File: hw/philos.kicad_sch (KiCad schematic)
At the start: 3 parts, among them U1 8086_Min_Mode, U2 SN74AHC574N, U3 SN74AHC574N

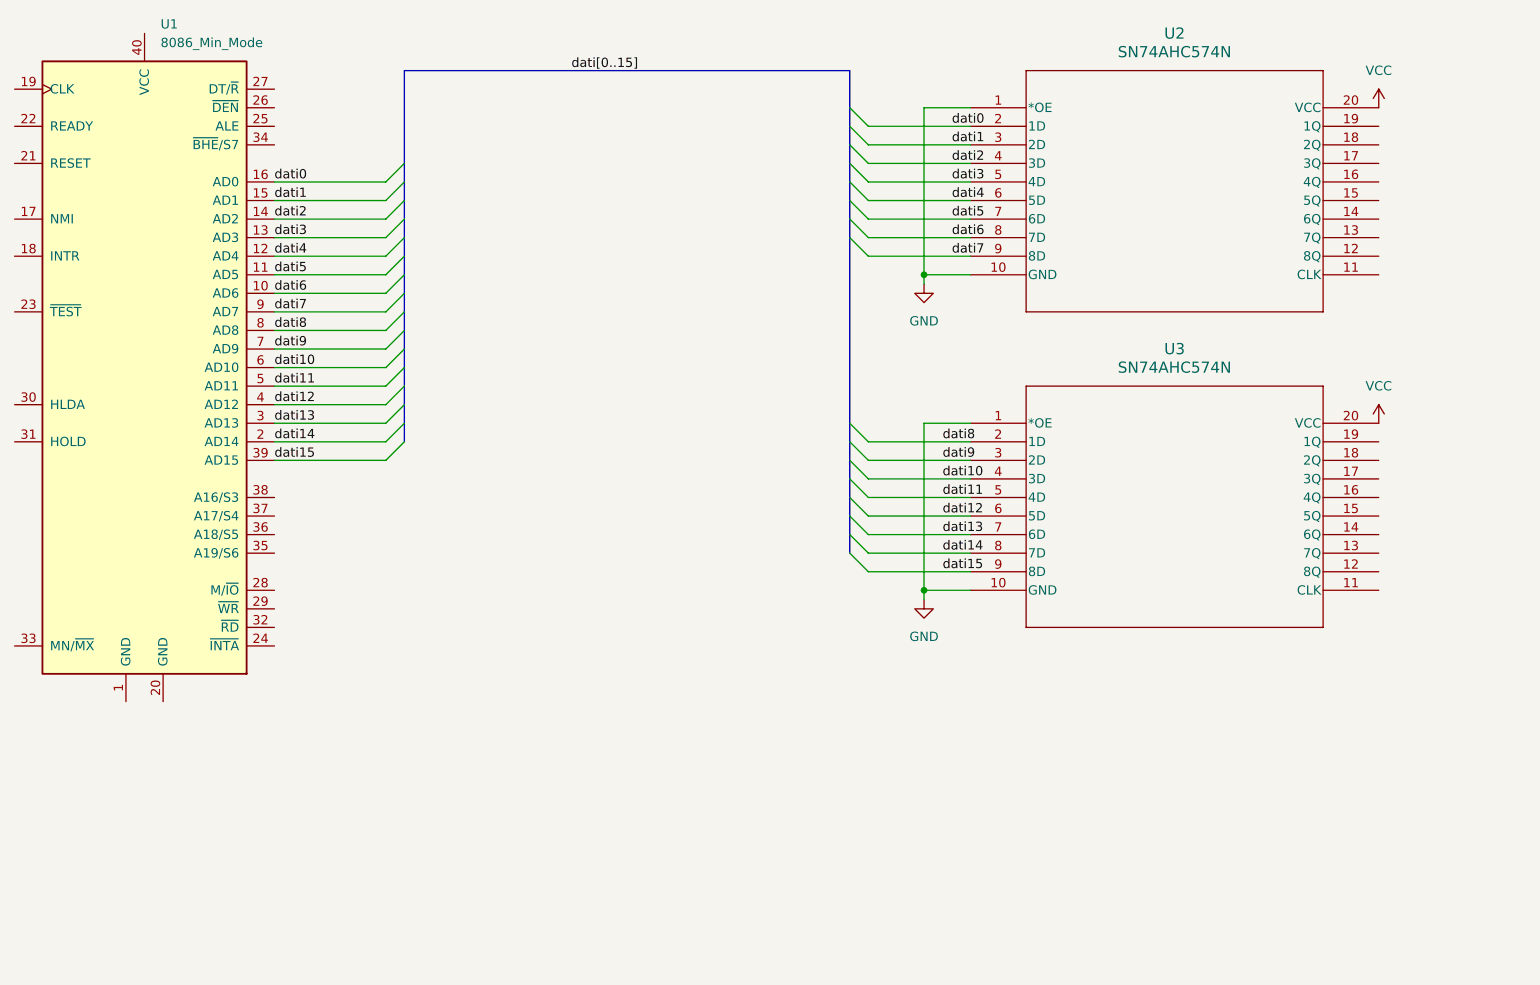
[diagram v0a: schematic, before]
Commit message: hw: Update to Kicad 9.0; Create makefile prototype; Remove batch script
The makefile is still in beta, needs more work

Signed-off-by: Matteo Bertolino <m.bertolino.m@gmail.com>
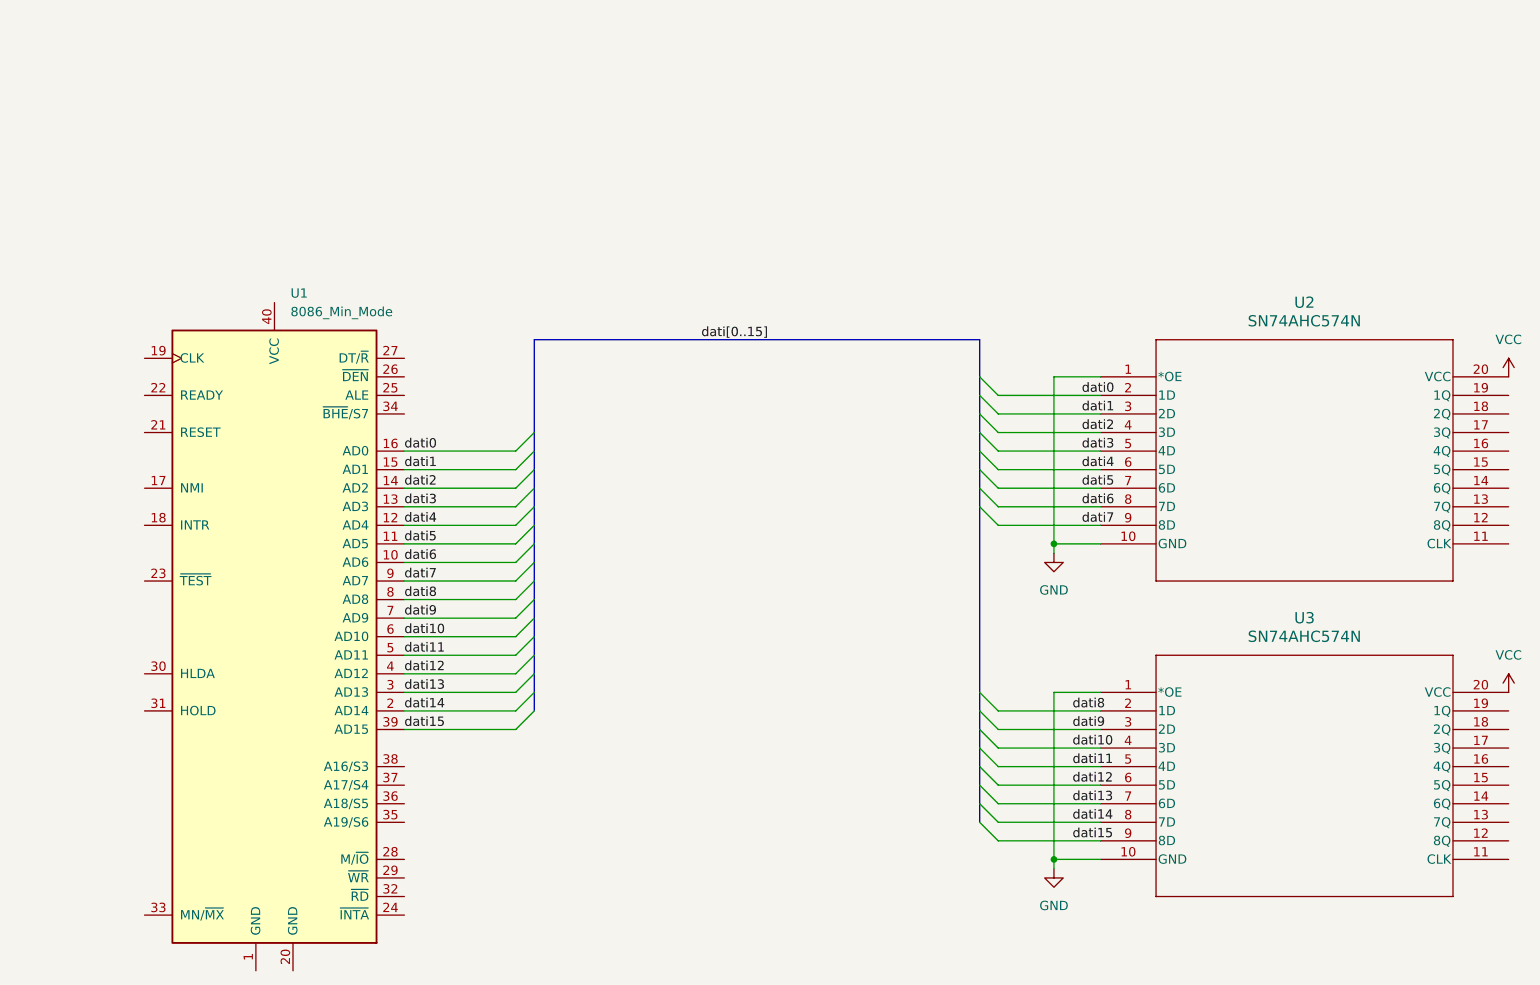
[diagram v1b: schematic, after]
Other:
- title: (none) -> philOS
- moved on the sheet: U1, U2, U3

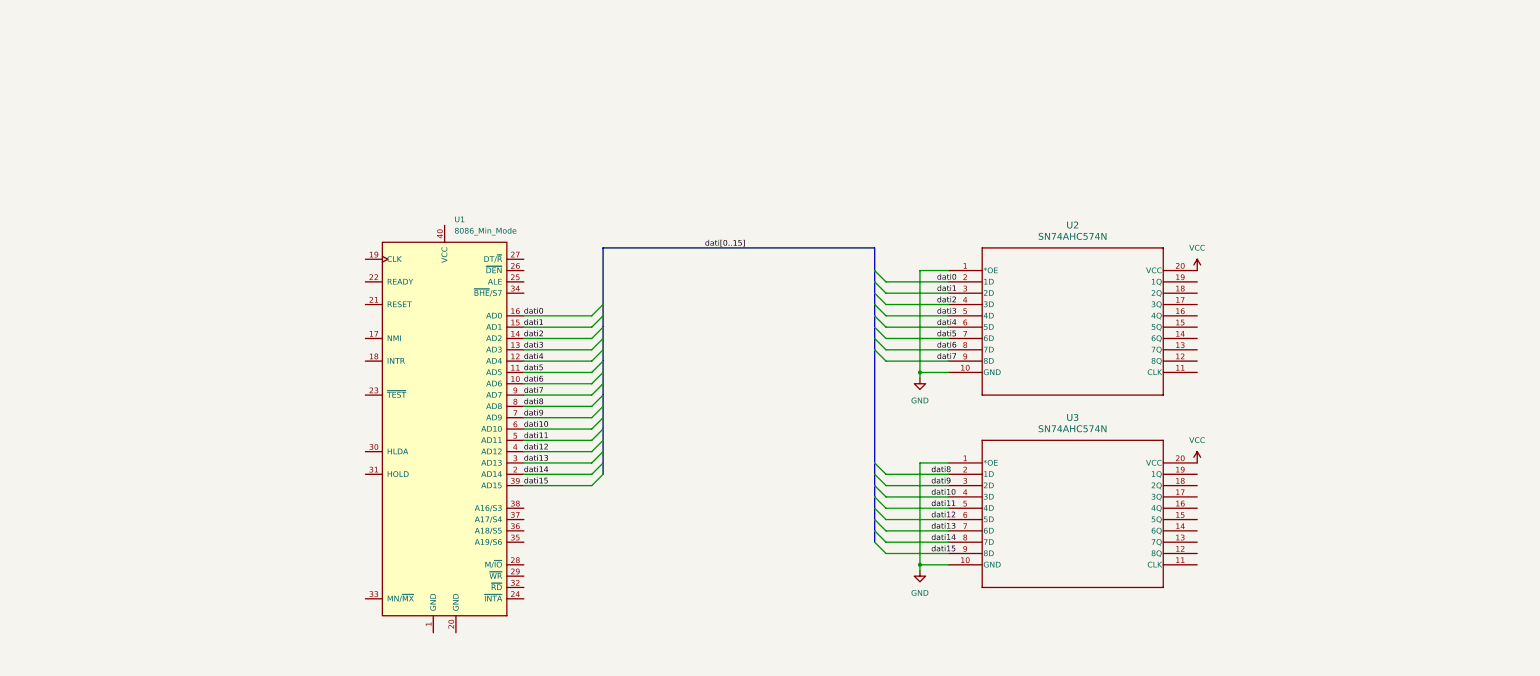
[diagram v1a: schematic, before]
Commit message: hw: add EEPROM and clock with respective footprints and symbols in diagram
No connection between component has been made yet

Signed-off-by: Matteo Bertolino <m.bertolino.m@gmail.com>
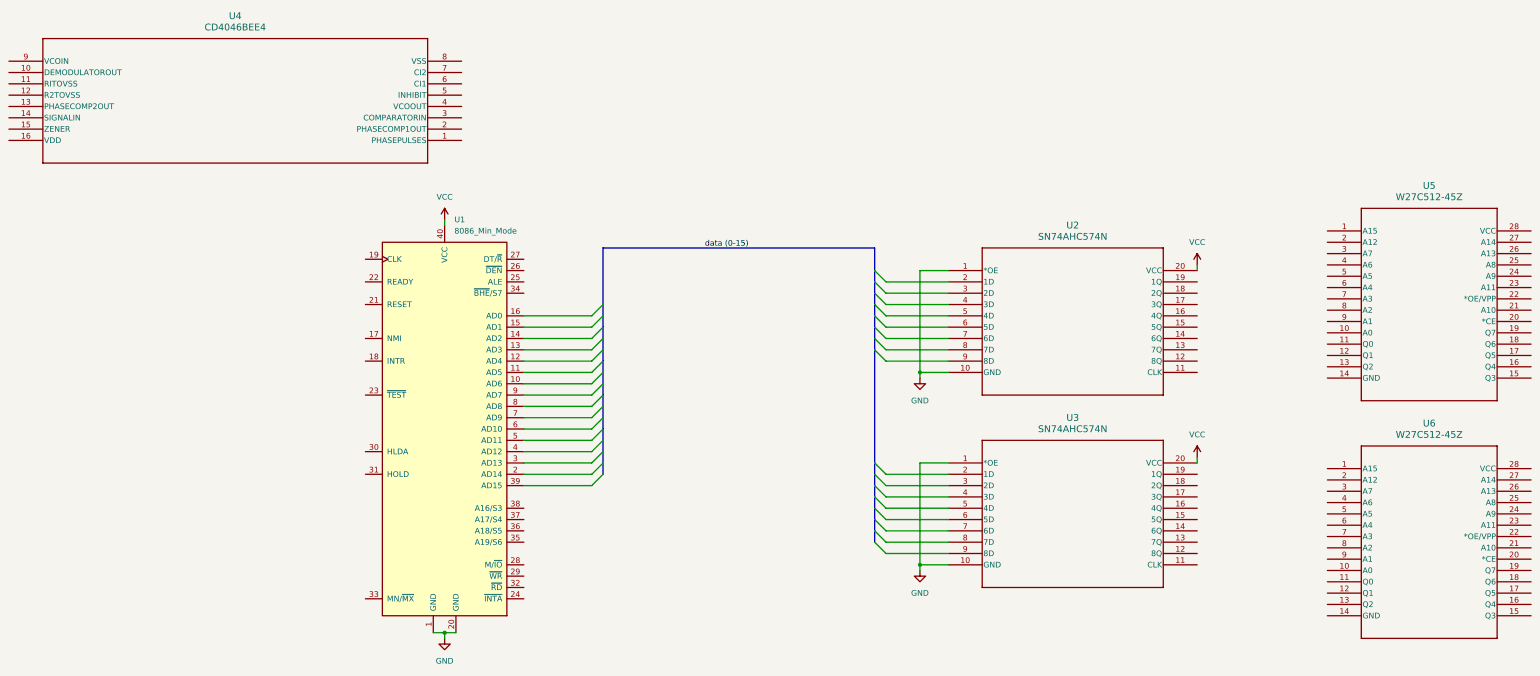
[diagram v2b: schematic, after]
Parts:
- added U4: CD4046BEE4, N16, symbol CD4046BEE4:CD4046BEE4
- added U5, U6: W27C512-45Z, 28P-DIP, symbol W27C512-45Z:W27C512-45Z
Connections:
- net GND: now also U1.1 (GND), U1.20 (GND)
- net VCC: now also U1.40 (VCC)
- net dati0: no longer names the net of U2.2 (1D)
- net dati0: no longer U1.16 (AD0)
- net dati1: no longer names the net of U2.3 (2D)
- net dati1: no longer U1.15 (AD1)
- net dati10: no longer names the net of U3.4 (3D)
- net dati10: no longer U1.6 (AD10)
- net dati11: no longer names the net of U3.5 (4D)
- net dati11: no longer U1.5 (AD11)
- net dati12: no longer names the net of U3.6 (5D)
- net dati12: no longer U1.4 (AD12)
- net dati13: no longer names the net of U3.7 (6D)
- net dati13: no longer U1.3 (AD13)
- net dati14: no longer names the net of U3.8 (7D)
- net dati14: no longer U1.2 (AD14)
- net dati15: no longer names the net of U3.9 (8D)
- net dati15: no longer U1.39 (AD15)
- net dati2: no longer names the net of U2.4 (3D)
- net dati2: no longer U1.14 (AD2)
- net dati3: no longer names the net of U2.5 (4D)
- net dati3: no longer U1.13 (AD3)
- net dati4: no longer names the net of U2.6 (5D)
- net dati4: no longer U1.12 (AD4)
- net dati5: no longer names the net of U2.7 (6D)
- net dati5: no longer U1.11 (AD5)
- net dati6: no longer names the net of U2.8 (7D)
- net dati6: no longer U1.10 (AD6)
- net dati7: no longer names the net of U2.9 (8D)
- net dati7: no longer U1.9 (AD7)
- net dati8: no longer names the net of U3.2 (1D)
- net dati8: no longer U1.8 (AD8)
- net dati9: no longer names the net of U3.3 (2D)
- net dati9: no longer U1.7 (AD9)

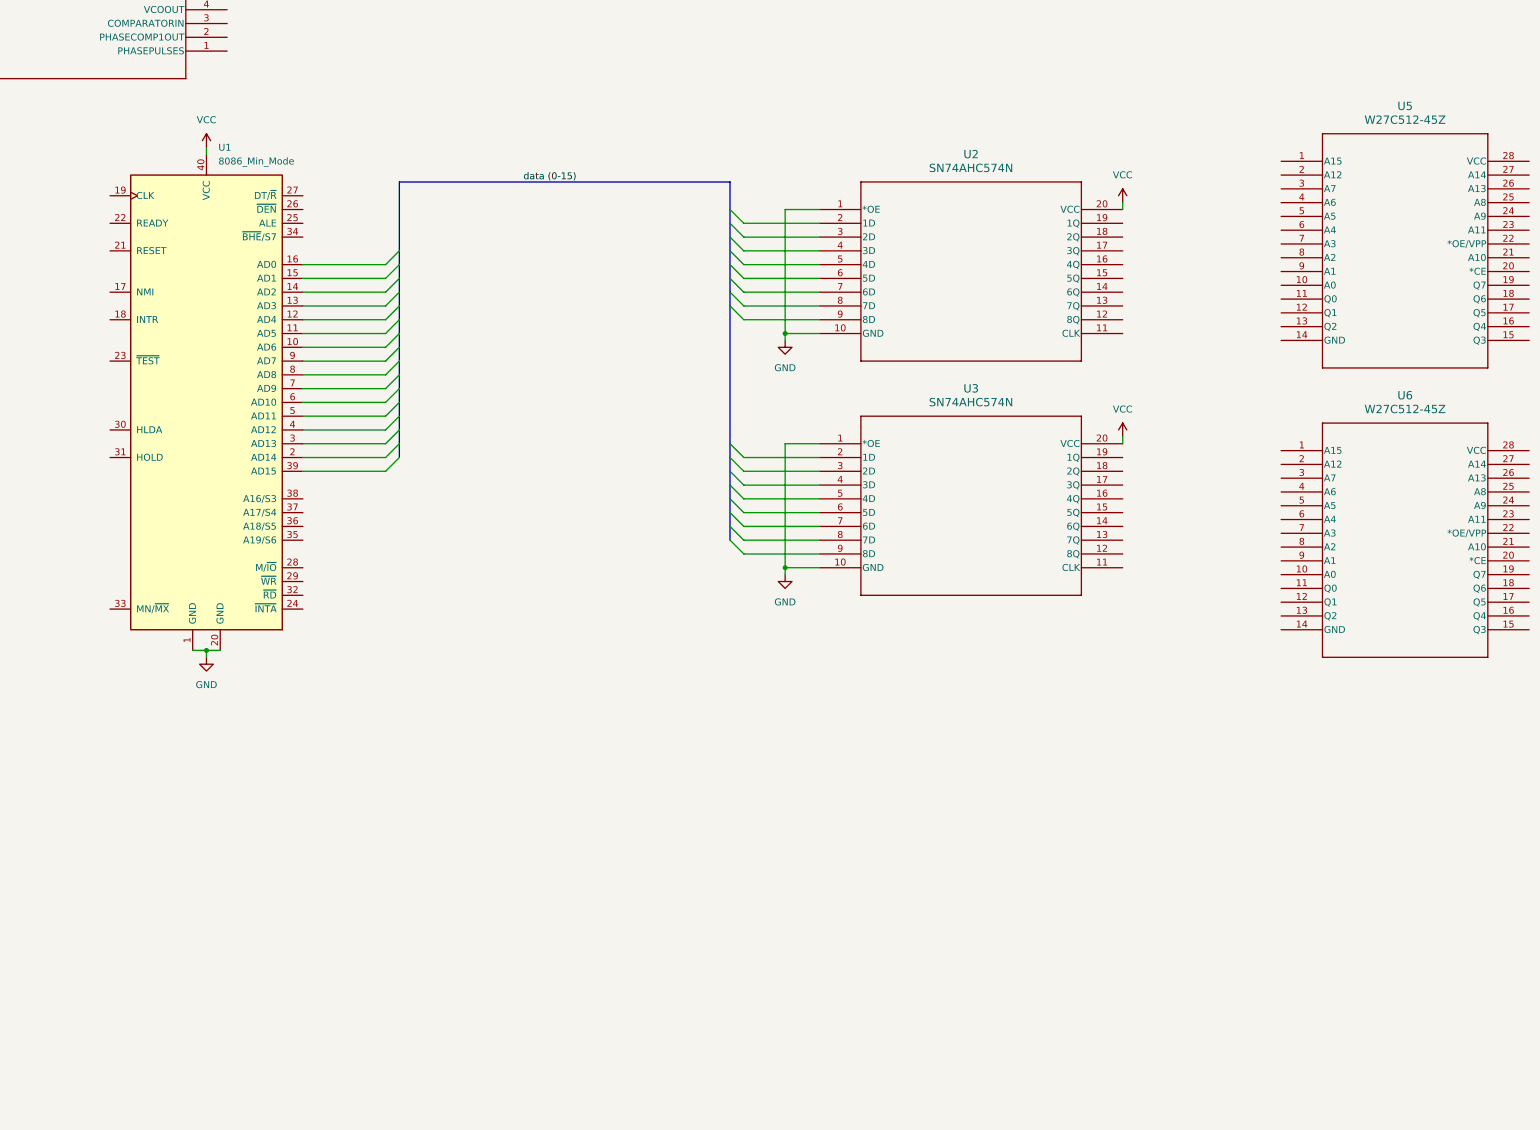
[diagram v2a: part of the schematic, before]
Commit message: hw: modified the latchers
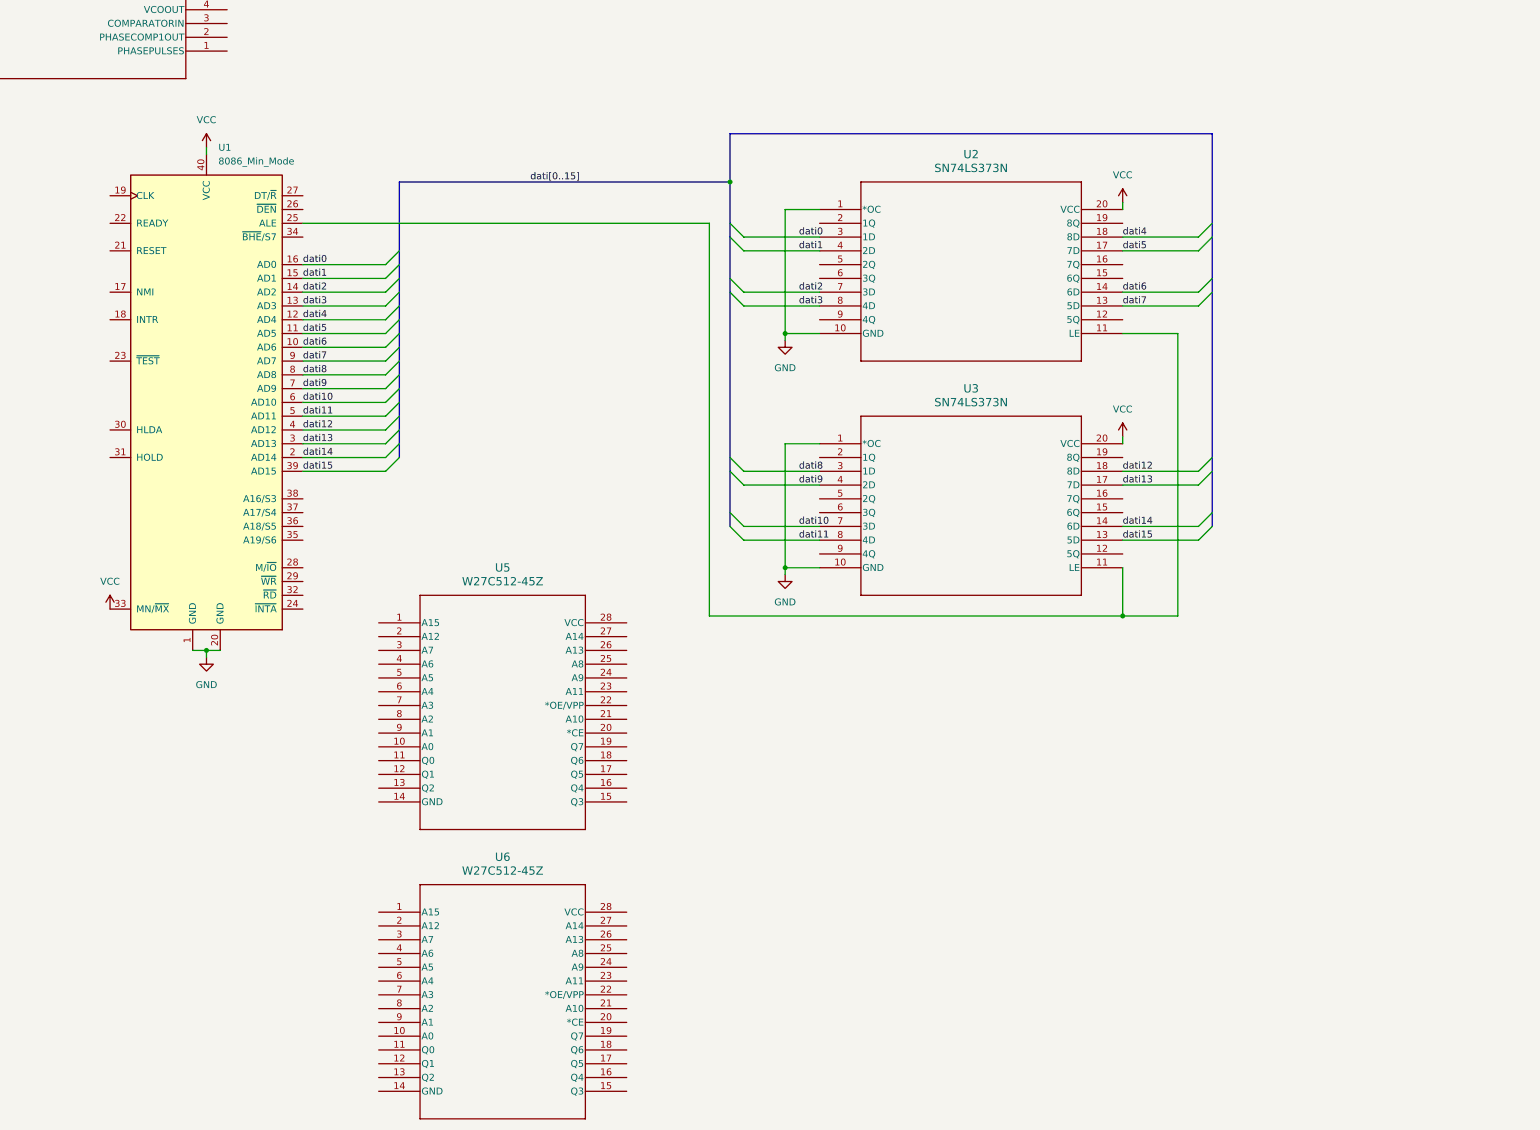
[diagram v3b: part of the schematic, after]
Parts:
- removed U2, U3: SN74AHC574N, N20, symbol SN74AHC574N:SN74AHC574N
- added U2, U3: SN74LS373N, N20, symbol SN74LS373N:SN74LS373N
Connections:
- net GND: now also U2.1 (*OC), U2.10 (GND), U3.1 (*OC), U3.10 (GND)
- net VCC: now also U1.33 (MN/~{MX}), U2.20 (VCC), U3.20 (VCC)
- net dati6: now reaches U1.10 (AD6)
- net dati6: now also U2.14 (6D)
- net dati5: now reaches U1.11 (AD5)
- net dati5: now also U2.17 (7D)
- net dati4: now reaches U1.12 (AD4)
- net dati4: now also U2.18 (8D)
- net dati3: now reaches U1.13 (AD3)
- net dati3: now also U2.8 (4D)
- net dati2: now reaches U1.14 (AD2)
- net dati2: now also U2.7 (3D)
- net dati1: now reaches U1.15 (AD1)
- net dati1: now also U2.4 (2D)
- net dati0: now reaches U1.16 (AD0)
- net dati0: now also U2.3 (1D)
- net dati14: now reaches U1.2 (AD14)
- net dati14: now also U3.14 (6D)
- net at U1.25 (ALE): now also U2.11 (LE), U3.11 (LE)
- net dati13: now reaches U1.3 (AD13)
- net dati13: now also U3.17 (7D)
- net dati15: now reaches U1.39 (AD15)
- net dati15: now also U3.13 (5D)
- net dati12: now reaches U1.4 (AD12)
- net dati12: now also U3.18 (8D)
- net dati11: now reaches U1.5 (AD11)
- net dati11: now also U3.8 (4D)
- net dati10: now reaches U1.6 (AD10)
- net dati10: now also U3.7 (3D)
- net dati9: now reaches U1.7 (AD9)
- net dati9: now also U3.4 (2D)
- net dati8: now reaches U1.8 (AD8)
- net dati8: now also U3.3 (1D)
- net dati7: now reaches U1.9 (AD7)
- net dati7: now also U2.13 (5D)
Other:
- moved on the sheet: U5, U6
